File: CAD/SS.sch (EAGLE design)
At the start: 84 parts, among them Q1 SN74AHC-NOR, Q2 UMD5N, Q4 SN74AHC-AND, Q5 BFP460, Q6 L78L05, Q7 NCP553, T1 MMBTRA104SS

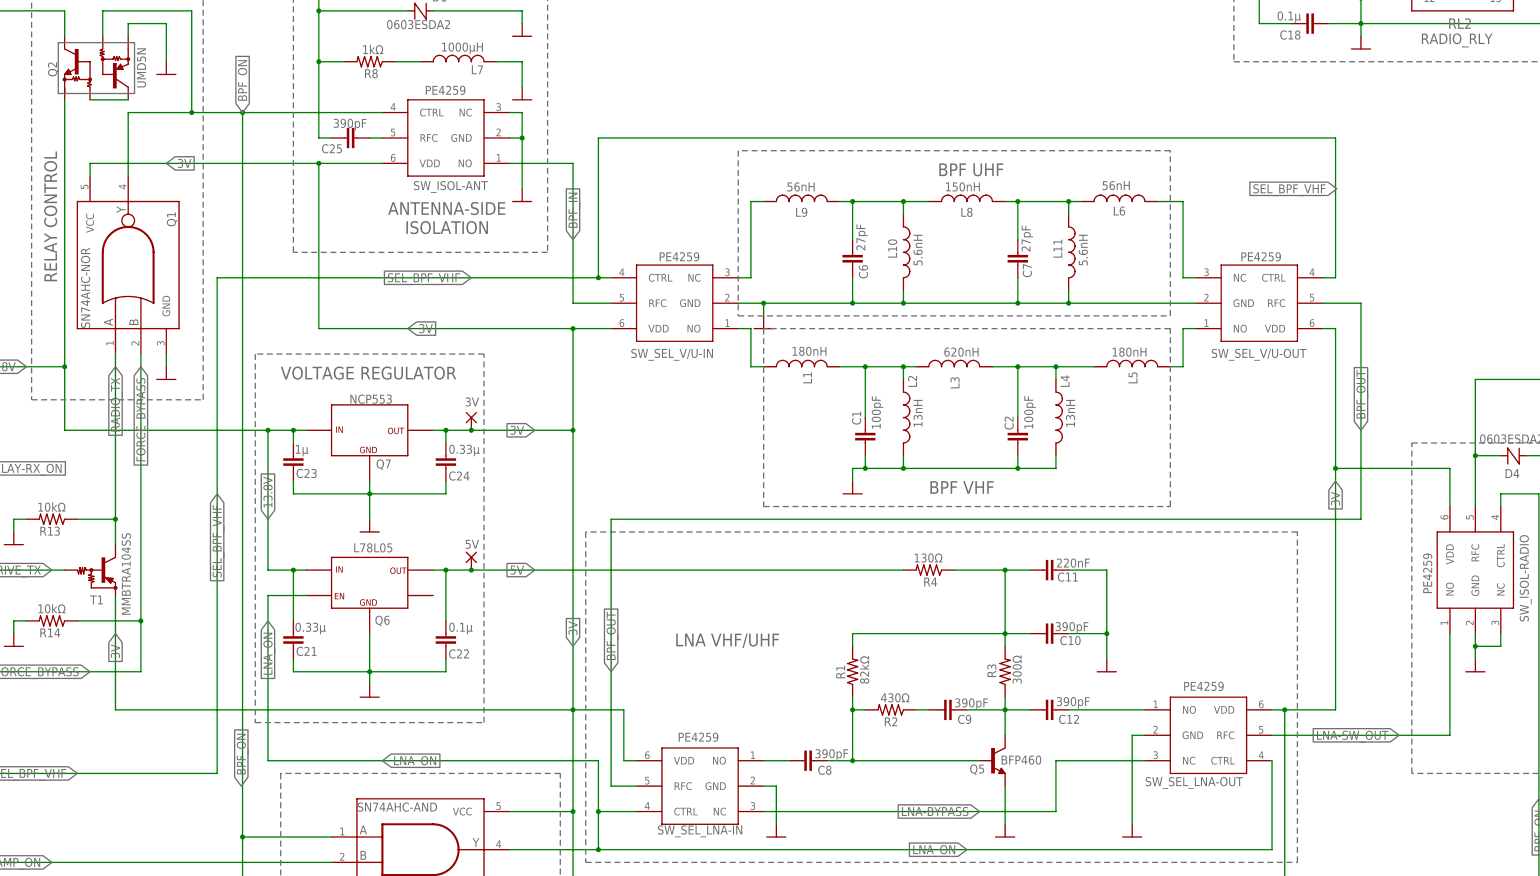
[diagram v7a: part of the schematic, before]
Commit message: SignalSurge: Several improvements (check comment for details)
* Changed the VHF BPF topology, using an impedance transformer to
  use a 1000 ohm-calculated BPF, yielding less critical component values
* Small improvements in BPF CPWs
* Implemented some changes suggested at r/rfElectronics
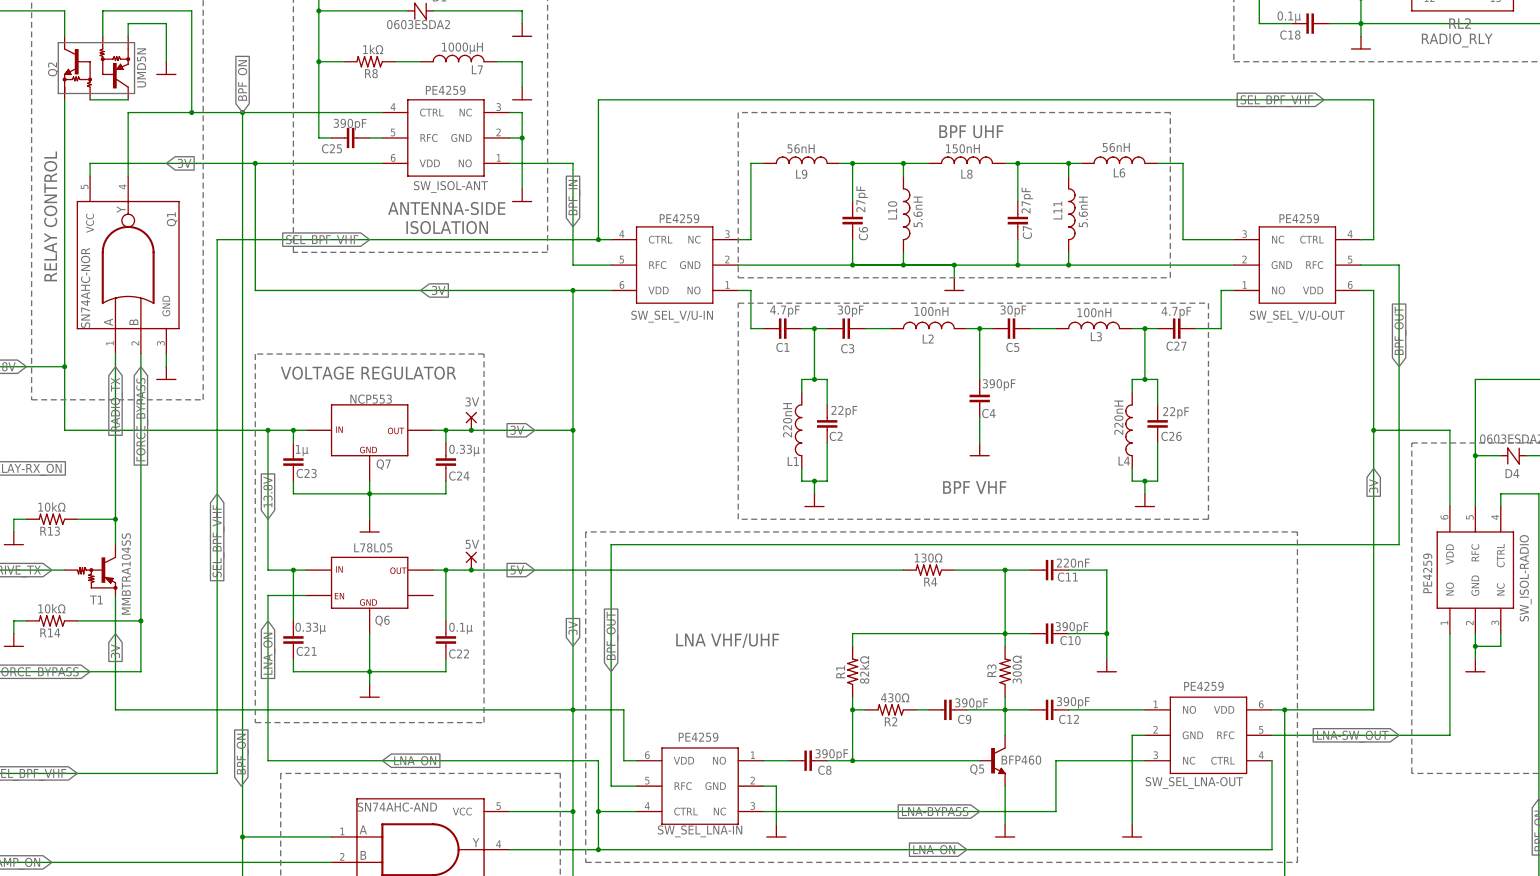
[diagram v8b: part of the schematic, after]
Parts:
- removed L5: 180nH, aarf:L-0805
- added C26: 22pF, aarf:MURATACAP
- added C27: 4.7pF, aarf:MURATACAP
- added C3, C5: 30pF, aarf:MURATACAP
- added C4: 390pF, aarf:MURATACAP
- C1: value 100pF -> 4.7pF
- C2: value 100pF -> 22pF
- L1: value 180nH -> 220nH
- L2: value 13nH -> 100nH
- L3: value 620nH -> 100nH
- L4: value 13nH -> 220nH
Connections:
- new net N$19: C5.2, L3.1
- new net N$4: C1.1, C2.1, C3.2, L1.2
- new net N$6: C4.1, C5.1, L2.2
- net GND: now also C2.2, C26.2, C4.2, L1.1; no longer C1.1, C2.1, L2.2
- net N$14: now also C26.1, C27.1; no longer C2.2, L5.1
- net N$5: now also C3.1; no longer C1.2, L1.2, L3.1
- net VHF-IN: now also C1.2; no longer L1.1
- net VHF-OUT: now also C27.2; no longer L5.2
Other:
- moved on the sheet: C1, C2, C6, C7, L1, L10, L11, L2, L3, L4, L6, L8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
